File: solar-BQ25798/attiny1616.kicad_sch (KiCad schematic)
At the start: 14 parts, among them J1901 Conn_01x04, U1901 ATtiny1616-M

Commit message: BQ25798 WIP
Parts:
- added BUZZER1901: MLT-7525, cacophony-library:BUZ-SMD_4P-L7.5-W7.5-P7.59-TL, symbol cacophony-library:MLT-7525
- added C1901: 1uF, Capacitor_SMD:C_0402_1005Metric, symbol Device:C
- added C1902: 10uF, Capacitor_SMD:C_0603_1608Metric, symbol Device:C_Small
- added R1901: 180Ω, Resistor_SMD:R_0402_1005Metric, symbol Device:R
- added U1901: AHT20_C2757850, cacophony-library:SENSOR-SMD_L3.0-W3.0-P1.00-BR, symbol cacophony-library:AHT20_C2757850
- renumbered C1901 to C1903, R1901 to R1902, R1902 to R1903, TP1910 to TP1901, TP1909 to TP1902, TP1908 to TP1903, TP1907 to TP1904, TP1906 to TP1905, TP1905 to TP1906, TP1904 to TP1907, TP1903 to TP1908, U1901 to U1902
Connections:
- net GND: now also C1901.2, C1902.2, U1901.5 (GND)
- net SCL: now also U1901.3 (SCL)
- net SDA: now also U1901.4 (SDA)
- new net +3V3: C1901.1, R1901.1
- new net AHT21_VDD: C1902.1, R1901.2, U1901.2 (VDD)
- no-connect marks 0 -> 2
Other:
- note added: "I2C Address 0x38"
- note added: "Temp and Humidity Sensor"

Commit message: Solar battery WIP
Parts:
- removed BUZZER1901: MLT-7525, cacophony-library:BUZ-SMD_4P-L7.5-W7.5-P7.59-TL, symbol cacophony-library:MLT-7525
- removed C1901: 1uF, Capacitor_SMD:C_0402_1005Metric, symbol Device:C
- removed J1901: Conn_01x04, Connector_PinHeader_2.00mm:PinHeader_1x04_P2.00mm_Vertical, symbol Connector_Generic:Conn_01x04
- removed TP1903, TP1904, TP1908: TestPoint, cacophony-library:TP_PAD, symbol cacophony-library:TestPoint
- added BUZZER1902: PS1240P02CT3, cacophony-library:BUZ-TH_BD12.5-P5.00-D0.9, symbol cacophony-library:PS1240P02CT3
- added D1901: D, Diode_SMD:D_SOD-323_HandSoldering, symbol Device:D
- added J1901: TC2030, Connector:Tag-Connect_TC2030-IDC-NL_2x03_P1.27mm_Vertical, symbol Connector:TC2030
- added Q1901: 2N7002, Package_TO_SOT_SMD:SOT-23, symbol Transistor_FET:2N7002
- added R1901, R1902: 10k, Resistor_SMD:R_0402_1005Metric, symbol Device:R
- added R1904: 0Ω, Resistor_SMD:R_0805_2012Metric, symbol Device:R
- added TP1906, TP1907: TestPoint, cacophony-library:TP_PAD, symbol cacophony-library:TestPoint
- renumbered C1903 to C1901, D1901 to D1902, R1902 to R1903, R1903 to R1905, R1901 to R1906, TP1906 to TP1901, TP1907 to TP1902, TP1901 to TP1903, TP1902 to TP1904, U1902 to U1901, U1901 to U1902
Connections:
- net +3V3 is gone; now on net +3.3V: R1906.1
- net +3.3V: now also R1901.2, R1902.2
- net GND: now also J1901.5, Q1901.2 (S)
- net RX: now also J1901.1
- net SCL: now also R1902.1
- net SDA: now also R1901.1
- net TX: now also J1901.3
- net UPDI: now also J1901.6
- net ~{INT}: now also U1901.1 (PA2); no longer U1901.5 (PA4)
- net LED_PHY: now reaches R1905.1, U1901.9 (PB5)
- net LED: now reaches D1902.2 (A), R1905.2
- net PULL_SENSE_LOW: now reaches U1901.18 (PC3)
- net BUZZER: now reaches U1901.2 (PA3)
- net BUZZER: now also Q1901.1 (G)
- net at TP1902.1: now also U1901.5 (PA4); no longer U1901.1 (PA2)
- net SENSE_DIV: now reaches U1901.17 (PC2)
- net AHT21_VDD renamed AHT20_VDD
- new net: BUZZER1902.2, D1901.2 (A), R1904.1
- new net: Q1901.3 (D), R1904.2
- new net: J1901.2, TP1906.1
- new net: J1901.4, TP1907.1
- new net PRE_LIN_REG: BUZZER1902.1 (+), D1901.1 (K)
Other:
- note added: "C94598"
- moved on the sheet: C1901, C1902, D1902, R1903, R1905, TP1901, TP1902, TP1903, TP1904, TP1905, U1901, U1902

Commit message: Version v0.0.2
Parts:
- D1901: LCSC Part (none) -> C2128
- Q1901: LCSC Part (none) -> C8545
- R1904: LCSC Part (none) -> C17477
- U1901: LCSC Part (none) -> C507118
- U1902: LCSC Part C2757850 -> C3012622
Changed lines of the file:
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@@
+			)
+		)
+		(property "LCSC Part" "C17477"
+			(at 71.12 102.87 0)
+			(effects
+				(font
+					(size 1.27 1.27)
+				)
+				(hide yes)
 			)
 		)
@@
 			)
 		)
+		(property "LCSC Part" "C8545"
+			(at 68.58 113.03 0)
+			(effects
+				(font
+					(size 1.27 1.27)
+				)
+				(hide yes)
+			)
+		)
 		(pin "1"
 		)
@@
 			)
 		)
+		(property "LCSC Part" "C2128"
+			(at 64.77 92.71 90)
+			(effects
+				(font
+					(size 1.27 1.27)
+				)
+				(hide yes)
+			)
+		)
 		(pin "2"
 		)
@@
 			)
 		)
+		(property "LCSC Part" "C507118"
+			(at 156.21 101.6 0)
+			(effects
+				(font
+					(size 1.27 1.27)
+				)
+				(hide yes)
+			)
+		)
 		(pin "1"
 		)
@@
 			)
 		)
-		(property "LCSC Part" "C2757850"
+		(property "LCSC Part" "C3012622"
 			(at 76.2 163.83 0)
 			(effects

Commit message: Tidy up of files
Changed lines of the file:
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@@
 	(text_box "This buzzer doesn't have an internal driver so we need to drive it with a PWM frequency around 2-3kHz\n"
 		(exclude_from_sim no)
-		(at 27.94 52.07 0)
+		(at 17.78 87.63 0)
 		(size 36.83 8.89)
 		(margins 0.9525 0.9525 0.9525 0.9525)

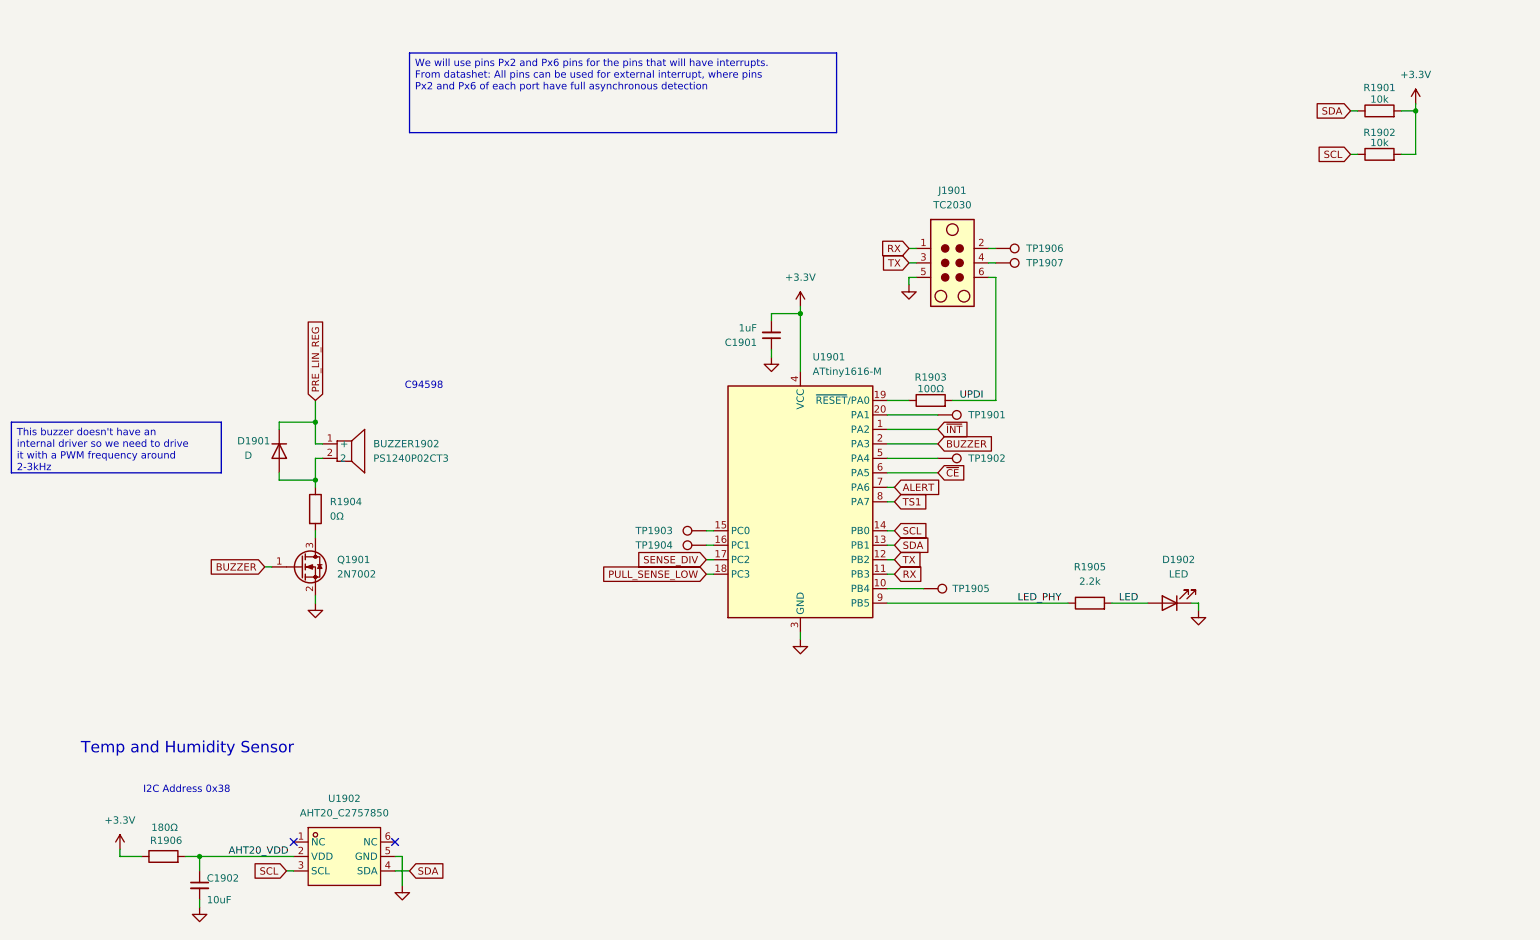
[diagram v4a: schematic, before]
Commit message: Update battery PCB
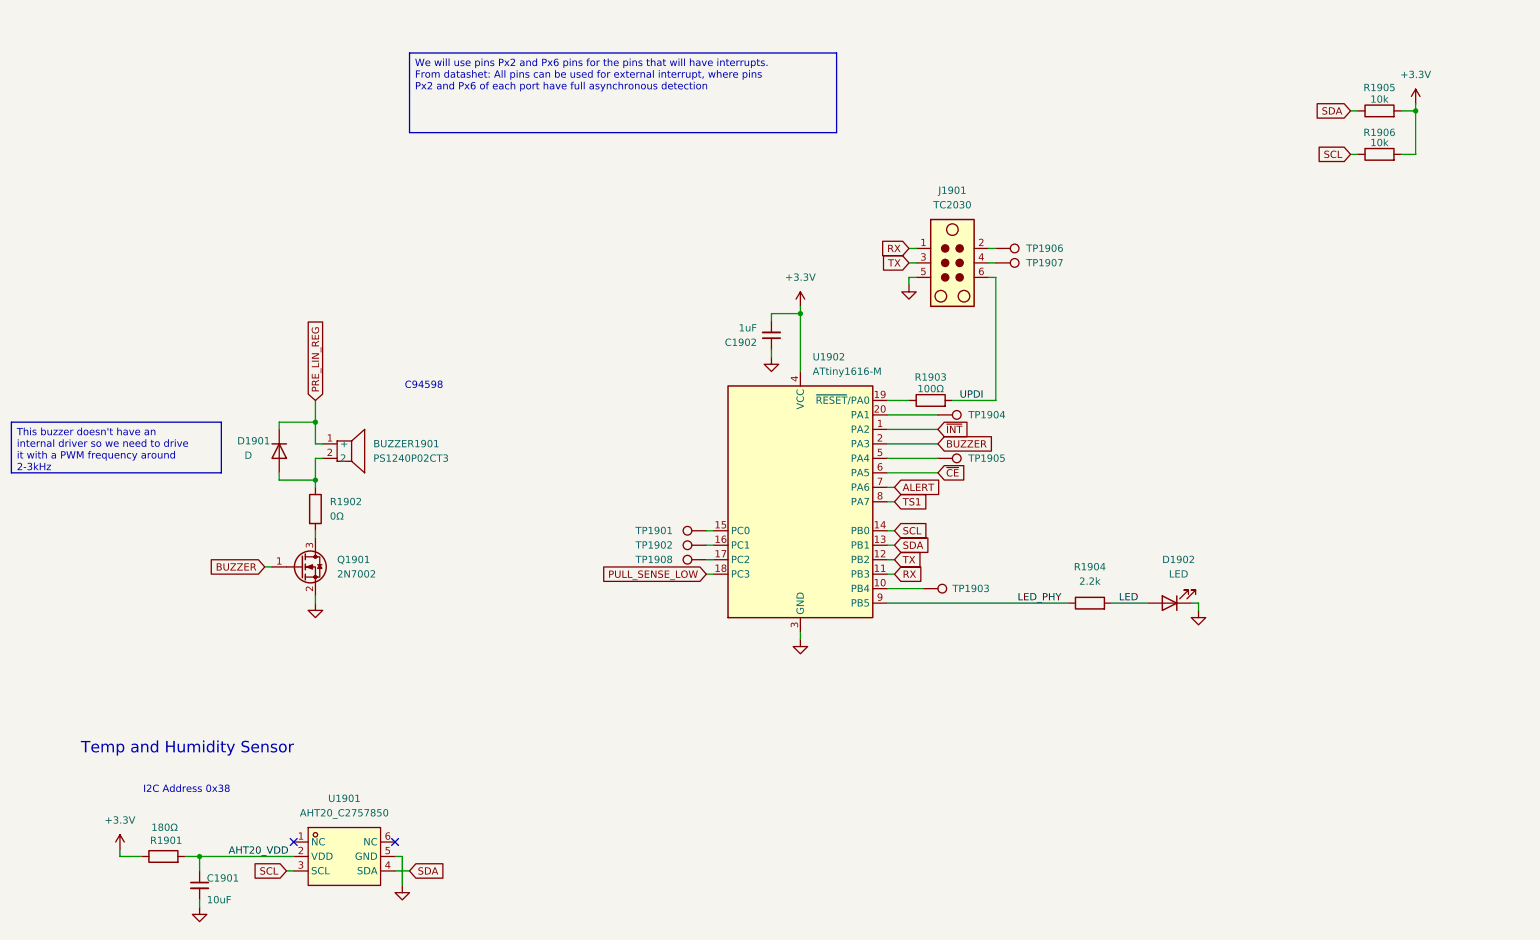
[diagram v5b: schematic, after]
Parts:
- added TP1908: TestPoint, cacophony-library:TP_PAD, symbol cacophony-library:TestPoint
- renumbered BUZZER1902 to BUZZER1901, C1902 to C1901, C1901 to C1902, R1906 to R1901, R1904 to R1902, R1905 to R1904, R1901 to R1905, R1902 to R1906, TP1903 to TP1901, TP1904 to TP1902, TP1905 to TP1903, TP1901 to TP1904, TP1902 to TP1905, U1902 to U1901, U1901 to U1902
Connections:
- net SENSE_DIV: no longer names the net of U1902.17 (PC2)
- net SENSE_DIV: now also TP1908.1

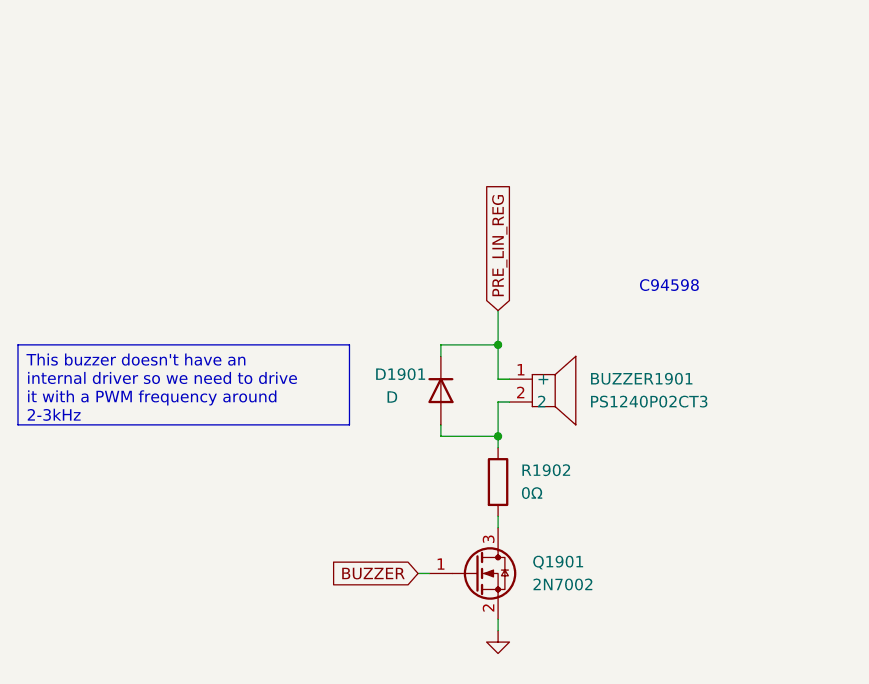
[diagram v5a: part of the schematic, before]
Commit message: Fix buzzer
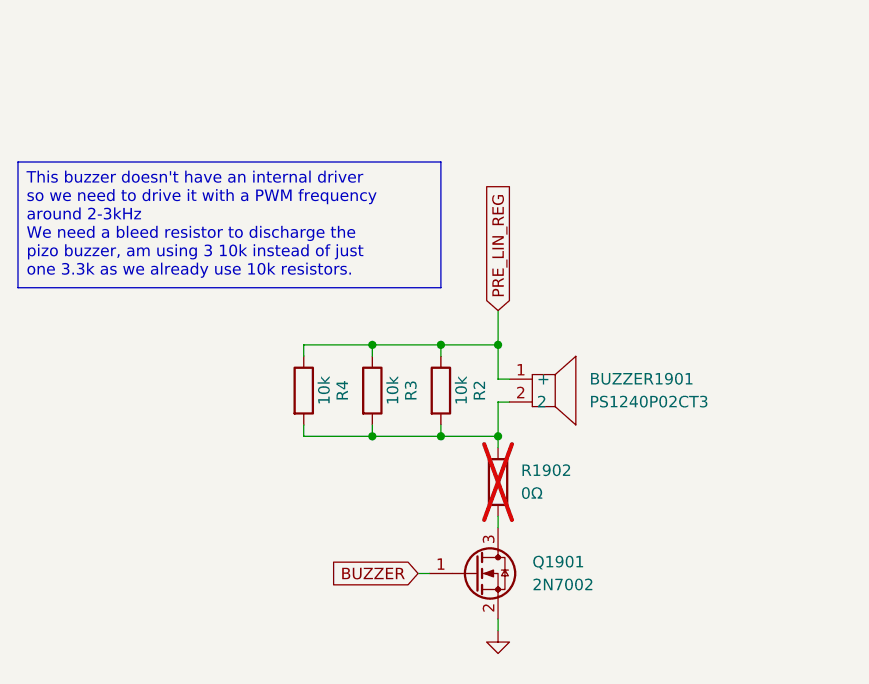
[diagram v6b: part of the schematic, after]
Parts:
- removed D1901: D, Diode_SMD:D_SOD-323_HandSoldering, symbol Device:D
- added R2, R3, R4: 10k, Resistor_SMD:R_0402_1005Metric, symbol Device:R
- R1902: footprint Resistor_SMD:R_0805_2012Metric -> cacophony-library:R_0805_0Ω_Short; LCSC Part C17477 -> (none); now not fitted; now left out of the parts list
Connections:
- net PRE_LIN_REG: now also R2.1, R3.1, R4.1
- net at BUZZER1901.2, R1902.1: now also R2.2, R3.2, R4.2
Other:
- note removed: "C94598"

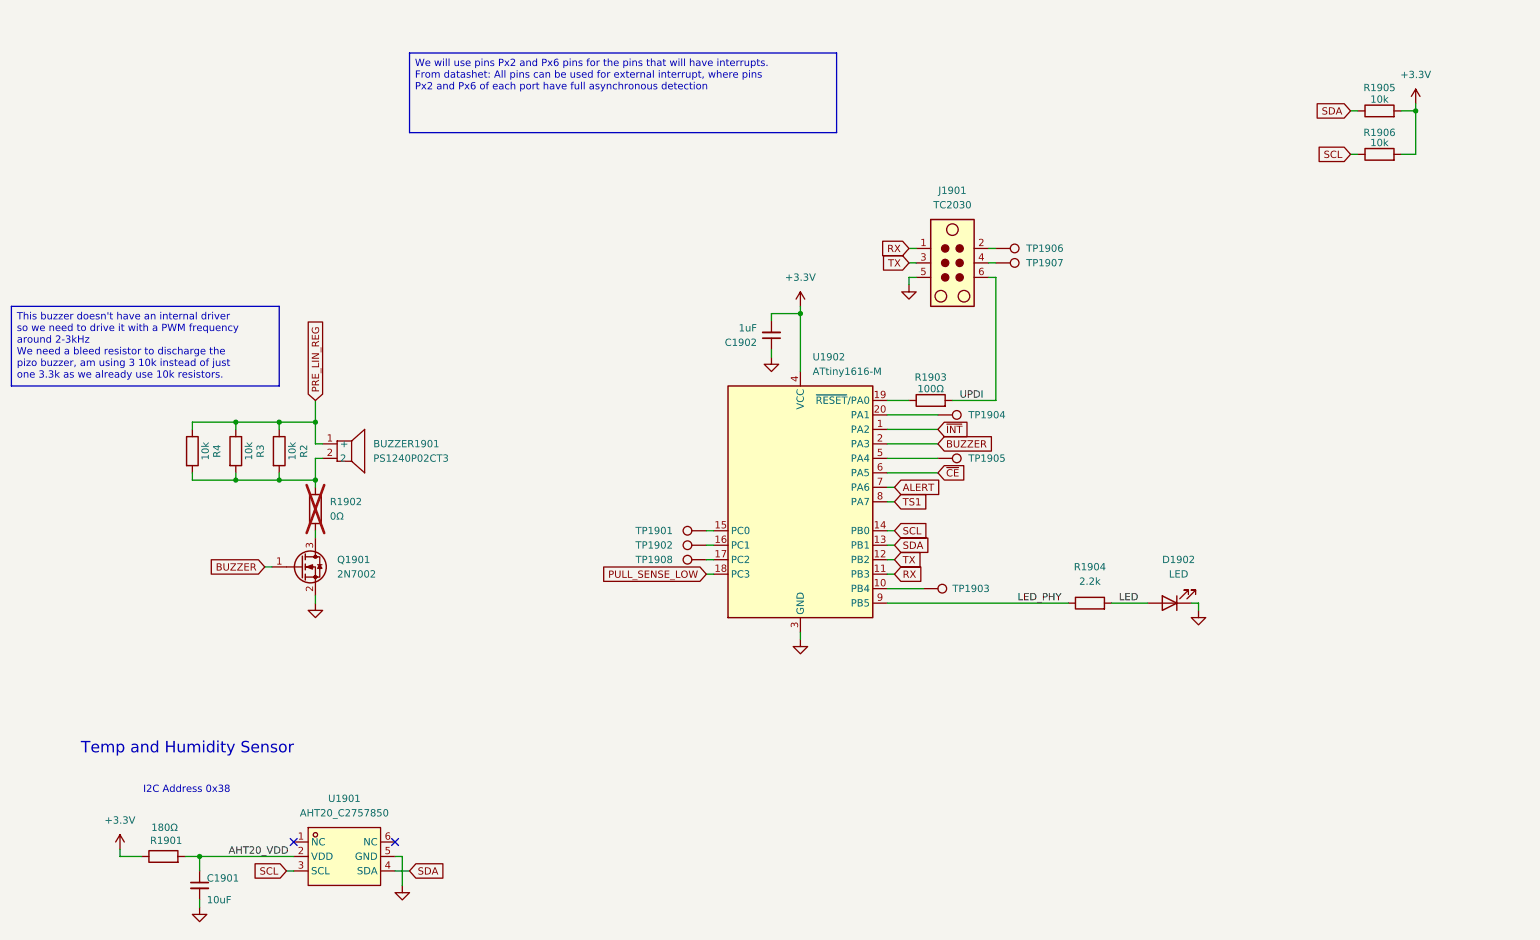
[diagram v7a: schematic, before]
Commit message: Fix pin for serial out and other small fixes
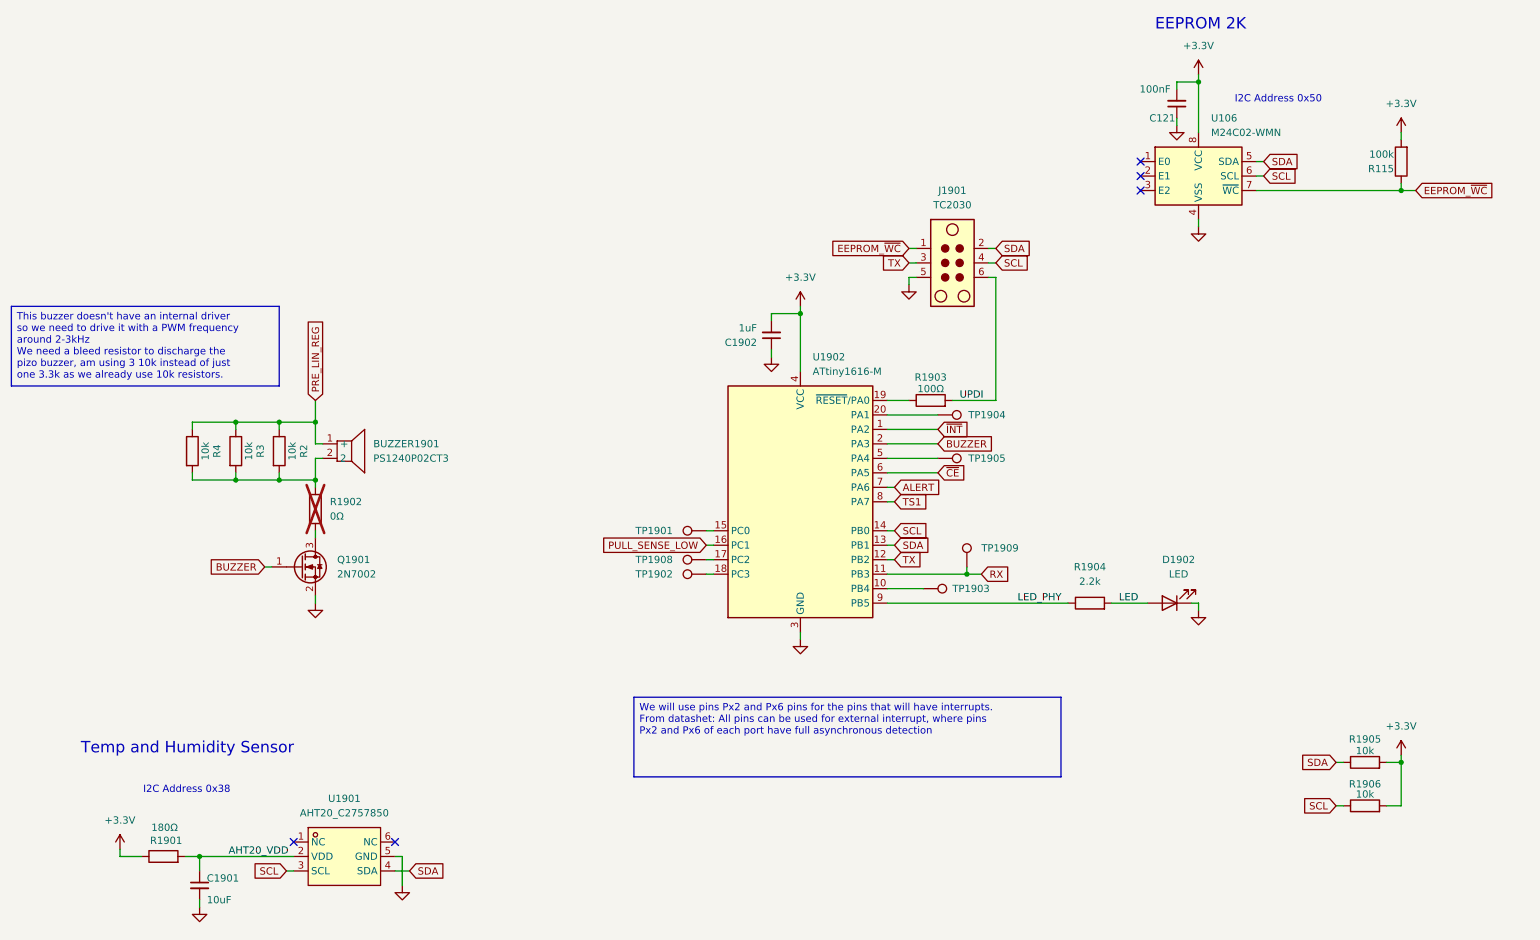
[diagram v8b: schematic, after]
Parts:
- removed TP1906, TP1907: TestPoint, cacophony-library:TP_PAD, symbol cacophony-library:TestPoint
- added C121: 100nF, Capacitor_SMD:C_0402_1005Metric, symbol Device:C_Small
- added R115: 100k, Resistor_SMD:R_0402_1005Metric, symbol Device:R
- added TP1909: TestPoint, cacophony-library:TP_PAD, symbol cacophony-library:TestPoint
- added U106: M24C02-WMN, Package_SO:SOIC-8_3.9x4.9mm_P1.27mm, symbol Memory_EEPROM:M24C02-WMN
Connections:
- net +3.3V: now also C121.2, R115.2, U106.8 (VCC)
- net GND: now also C121.1, U106.4 (VSS)
- net PULL_SENSE_LOW: now also U1902.16 (PC1); no longer U1902.18 (PC3)
- net RX: now also TP1909.1; no longer J1901.1
- net SCL: now also J1901.4, U106.6 (SCL)
- net SDA: now also J1901.2, U106.5 (SDA)
- net at TP1902.1: now also U1902.18 (PC3); no longer U1902.16 (PC1)
- new net EEPROM_~{WC}: J1901.1, R115.1, U106.7 (~{WC})
- no-connect marks 2 -> 5
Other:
- note added: "EEPROM 2K"
- note added: "I2C Address 0x50"
- moved on the sheet: R1905, R1906, TP1902
